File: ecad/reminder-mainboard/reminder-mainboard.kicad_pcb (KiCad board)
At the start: 2 copper layers, 65 x 30 mm, 26 parts, among them J1 0530470210, J10 0530470310, J12 0530470310, J13 0530470310, J14 Conn_02x04_Odd_Even, J15 0530470310, J16 Conn_01x03_Male, J17 Raspberry_Pi_2_3, J3 0530470310, J4 0530470210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

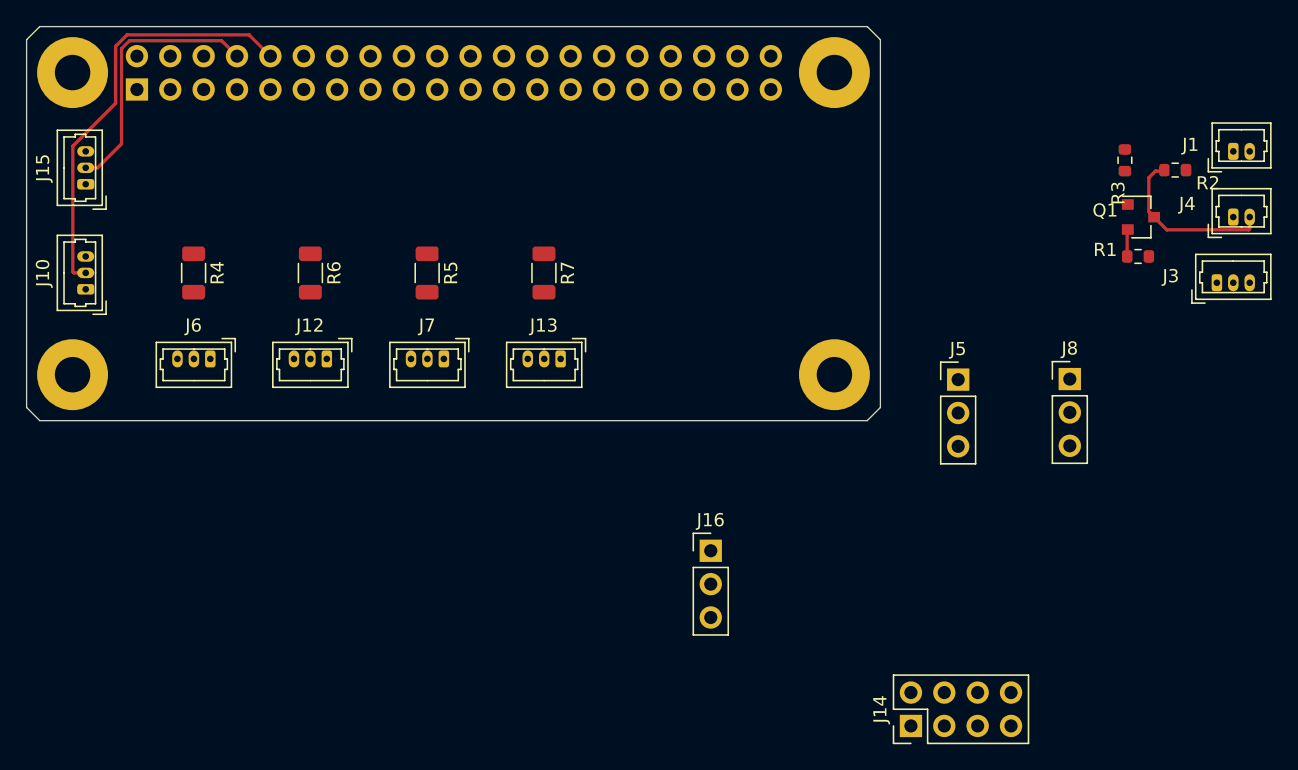
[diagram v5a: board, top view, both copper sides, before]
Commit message: Added LCSC part numbers, minor tweaks based on part availablity.
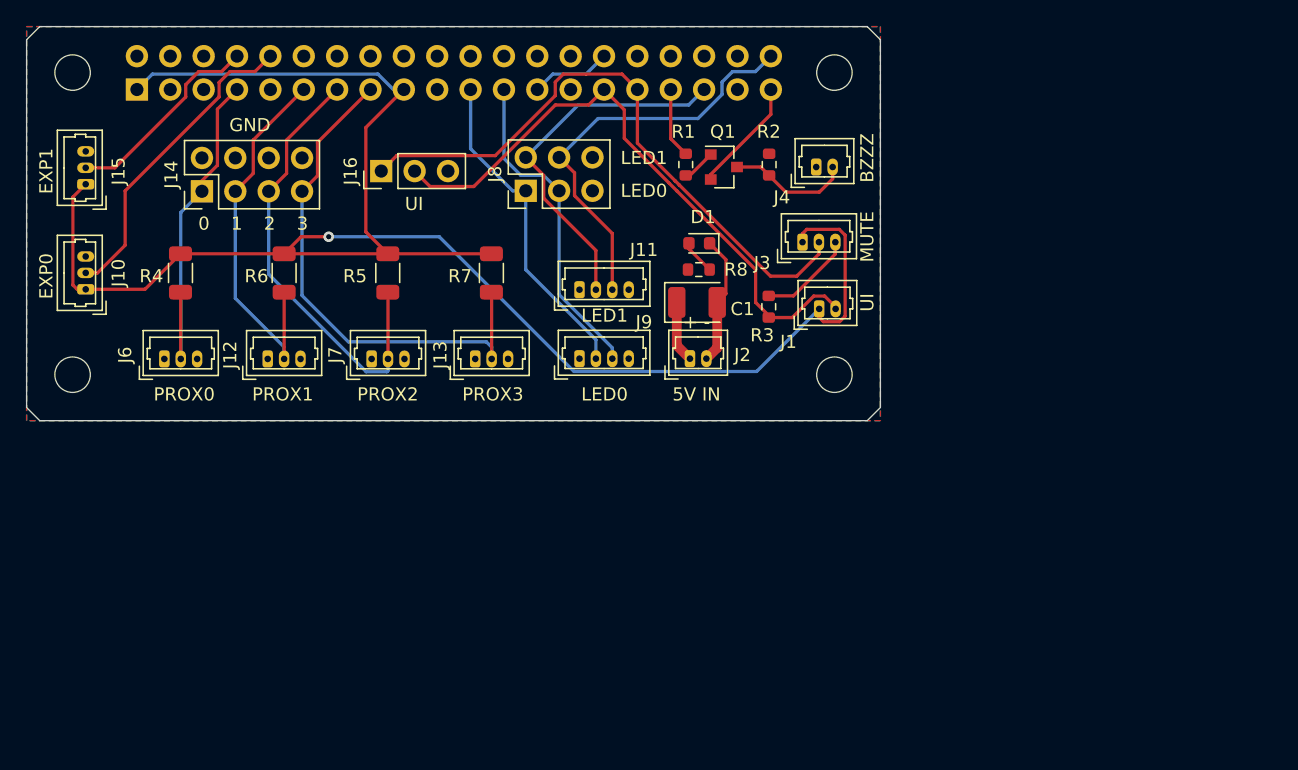
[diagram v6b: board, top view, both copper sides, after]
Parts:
- removed J5: Conn_01x03_Male, Connector_PinHeader_2.54mm:PinHeader_1x03_P2.54mm_Vertical
- added C1: 100uf, Capacitor_Tantalum_SMD:CP_EIA-3528-21_Kemet-B, F.Cu at (171.0, 110.0)
- added D1: 19-217/BHC-ZL1M2RY/3T, LED_SMD:LED_0603_1608Metric, F.Cu at (171.2, 105.5)
- added J11: 0530470410, Connector_Molex:Molex_PicoBlade_53047-0410_1x04_P1.25mm_Vertical, F.Cu at (162.1, 109.0)
- added J2: 0530470210, Connector_Molex:Molex_PicoBlade_53047-0210_1x02_P1.25mm_Vertical, F.Cu at (170.5, 114.3)
- added J9: 0530470410, Connector_Molex:Molex_PicoBlade_53047-0410_1x04_P1.25mm_Vertical, F.Cu at (162.1, 114.3)
- added R8: 120, Resistor_SMD:R_0603_1608Metric, F.Cu at (171.2, 107.5)
- H1, H2, H3, H4: footprint MountingHole:MountingHole_2.7mm_M2.5_Pad -> MountingHole:MountingHole_2.7mm_M2.5
- J8: value Conn_01x03_Male -> Conn_02x03_Male; footprint Connector_PinHeader_2.54mm:PinHeader_1x03_P2.54mm_Vertical -> Connector_PinHeader_2.54mm:PinHeader_2x03_P2.54mm_Vertical
- Q1: value 2N3904 -> S9013
- R1: value 510 -> 2.2k
- R2, R3: value 10k -> 11k
- R4, R5, R6, R7: value 15k -> 10k
- moved J14 67.6 mm to (133.3, 101.5)
- moved J8 43.8 mm to (158.0, 101.5), turned to 90 degrees
- moved J16 38.3 mm to (147.0, 100.0), turned to 90 degrees
- moved R1 35.1 mm to (170.2, 99.5), turned to 270 degrees
- moved J1 33.7 mm to (180.3, 110.5)
- moved J4 32.0 mm to (180.1, 99.7)
- moved Q1 32.0 mm to (173.1, 99.7)
- moved J3 31.7 mm to (179.1, 105.4)
- moved R2 30.9 mm to (176.5, 99.5), turned to 270 degrees
- moved R3 29.3 mm to (176.5, 110.3), turned to 90 degrees
- moved J13 6.50 mm to (154.2, 114.3), turned to 0 degrees
- moved J7 5.50 mm to (146.3, 114.3), turned to 0 degrees
- moved J12 4.50 mm to (138.4, 114.3), turned to 0 degrees
- moved R7 4.00 mm to (155.4, 107.8)
- moved J6 3.50 mm to (130.5, 114.3), turned to 0 degrees
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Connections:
- J8 pad 1: /LED1_SDO -> /LED0_SDO
- J8 pad 2: /LED1_SCK -> /LED1_SDO
- J8 pad 3: GND -> /LED0_SCK
- Q1 pad 1: GND -> Net-(Q1-Pad1)
- Q1 pad 2: Net-(Q1-Pad2) -> GND
- R1 pad 2: Net-(Q1-Pad2) -> Net-(Q1-Pad1)
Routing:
- net +3V3: track 0.00 -> 137.7 mm, vias 0 -> 1
- net /MUTE: track 0.00 -> 47.3 mm
- net /UI_BUTTON: track 0.00 -> 46.8 mm
- net /PROX3_OUT: track 0.00 -> 39.9 mm
- net /PROX2_OUT: track 0.00 -> 34.4 mm
- net GND: track 0.00 -> 32.1 mm
- net /LED1_SCK: track 0.00 -> 31.6 mm
- net /PROX1_OUT: track 0.00 -> 29.3 mm
- net /PROX0_OUT: track 0.00 -> 28.2 mm
- net /LED1_SDO: track 0.00 -> 28.0 mm
- net /LED0_SDO: track 0.00 -> 25.0 mm
- net /LED0_SCK: track 0.00 -> 24.9 mm
- net /EXP0: track 32.3 -> 24.0 mm
- net /BUZZER: track 0.00 -> 5.36 mm
- net +5V: track 0.00 -> 4.69 mm
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- added copper zone on F.Cu, net +5V
- added copper zone on B.Cu, net GND
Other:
- board text added: "+ -"
- board text added: "0"
- board text added: "1"
- board text added: "2"
- board text added: "3"
- board text added: "5V IN"
- board text added: "BZZZ"
- board text added: "EXP0"
- board text added: "EXP1"
- board text added: "GND"
- board text added: "JLCJLCJLCJLC"
- board text added: "LED0"
- board text added: "LED1"
- board text added: "MUTE"
- board text added: "PROX0"
- board text added: "PROX1"
- board text added: "PROX2"
- board text added: "PROX3"
- board text added: "UI"
- board text added: "med-reminder revA - JDG - 5.9.21"

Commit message: Created production files and gerbers
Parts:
- added G***: LOGO, Decals:tiny-penguin, F.Cu at (175.9, 116.2)
- added G***: LOGO, Decals:14mm-penguin, B.Cu at (170.2, 104.1)
